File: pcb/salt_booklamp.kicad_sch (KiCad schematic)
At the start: 26 parts, among them J1 USB-C31-S-RA-CS1E-BK-T/R, P1 PIC-TC2050-IDC, U1 PIC16F15213-I/SN, U2 BQ21040DBVR, U3 TPS61158DRVR

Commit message: Add CC resistors to schematic for USB compliant smart chargers
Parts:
- added R10, R9: 5k1, salt_booklamp_footprints:res_0603, symbol salt_booklamp:resistor
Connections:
- net GND: now also R10.2, R9.2
- net at J1.A5 (CC1): now also R9.1
- net at J1.B5 (CC2): now also R10.1
- no-connect marks 17 -> 15

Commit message: Changed 0603 parts to 0402, assigned 0402 uF cap MPN, still need to assign 0402 Resistor MPNs
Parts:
- C1, C2, C3, C4, C5: footprint salt_booklamp_footprints:cap_0603 -> Capacitor_SMD:C_0402_1005Metric; Manufacturer Part Number CL10B105KP8NNNC -> EMK105BJ105KV-F
- R1, R10, R2, R3, R4, R5, R6, R7, R8, R9: footprint salt_booklamp_footprints:res_0603 -> Resistor_SMD:R_0402_1005Metric
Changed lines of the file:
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@@
 		)
 	)
-	(text_box "PENDING CHANGES Rev 0.2\n----------------------\n[ ]-Measure Battery Voltage? - move measurement to different pin\n\n[X]-Add another LED\n\n[ ]-Battery Connector\n\n[X]-USBC - 5k1 R from CC to GND\n\n[ ]-0402 components for more space\n\n"
+	(text_box "PENDING CHANGES Rev 0.2\n----------------------\n[ ]-Measure Battery Voltage? - move measurement to different pin\n\n[X]-Add another LED\n\n[ ]-Battery Connector\n\n[X]-USBC - 5k1 R from CC to GND\n\n[X]-0402 components for more space\n\n"
 		(exclude_from_sim no)
 		(at 27.94 153.67 0)
@@
 			"AAAAAAAAAAAAAAAAAAAAAAAAAAAAAAAAAAAAAAAAAAAAAAAAAAAAAAAAAAAAAAAAAAAAAAAAAAAA"
 			"AAAAAAAAAAAAAAAAAAAAAAAAAAAAAAAAAAAAAAAAAAAAAAAAAAAAAAAAAAAAAAAAAAAAAAAAAAAA"
+			"AAAAAAAAAAAAAAAAAAAAAAAAAAAAAAAAAAAAAAAAAAAAAAAAAAAAAAAAAAAAAAAAAAAAAAAAAAAA"
+			"AAAAAAAAAAAAAAAAAAAAAAAAAAAAAAAAAAAAAAAAAAAAAAAAAAAAAAAAAAAAAAAAAAAAAAAAAAAA"
+			"AAAAAAAAAAAAAAAAAAAAAAAAAAAAAAAAAAAAAAAAAAAAAAAAAAAAAAAAAAAAAAAAAAAAAAAAAAAA"
+			"AAAAAAAAAAAAAAAAAAAAAAAAAAAAAAAAAAAAAAAAAAAAAAAAAAAAAAAAAAAAAAAAAAAAAAAAAAAA"
+			"AAAAAAAAAAAAAAAAAAAAAAAAAAAAAAAAAAAAAAAAAAAAAAAAAAAAAAAAAAAAAAAAAAAAAAAAAAAA"
+			"AAAAAAAAAAAAAAAAAAAAAAAAAAAAAAAAAAAAAAAAAAAAAAAAAAAAAAAAAAAAAAAAAAAAAAAAAAAA"
+			"AAAAAAAAAAAAAAAAAAAAAAAAAAAAAAAAAAAAAAAAAAAAAAAAAAAAAAAAAAAAAAAAAAAAAAAAAAAA"
+			"AAAAAAAAAAAAAAAAAAAAAAAAAAAAAAAAAAAAAAAAAAAAAAAAAAAAAAAAAAAAAAAAAAAAAAAAAAAA"
+			"AAAAAAAAAAAAAAAAAAAAAAAAAAAAAAAAAAAAAAAAAAAAAAAAAAAAAAAAAAAAAAAAAAAAAAAAAAAA"
+			"AAAAAAAAAAAAAAAAAAAAAAAAAAAAAAAAAAAAAAAAAAAAAAAAAAAAAAAAAAAAAAAAAAAAAAAAAAAA"
+			"AAAAAAAAAAAAAAAAAAAAAAAAAAAAAAAAAAAAAAAAAAAAAAAAAAAAAAAAAAAAAAAAAAAAAAAAAAAA"
+			"AAAAAAAAAAAAAAAAAAAAAAAAAAAAAAAAAAAAAAAAAAAAAAAAAAAAAAAAAAAAAAAAAAAAAAAAAAAA"
+			"AAAAAAAAAAAAAAAAAAAAAAAAAAAAAAAAAAAAAAAAAAAAAAAAAAAAAAAAAAAAAAAAAAAAAAAAAAAA"
+			"AAAAAAAAAAAAAAAAAAAAAAAAAAAAAAAAAAAAAAAAAAAAAAAAAAAAAAAAAAAAAAAAAAAAAAAAAAAA"
+			"AAAAAAAAAAAAAAAAAAAAAAAAAAAAAAAAAAAAAAAAAAAAAAAAAAAAAAAAAAAAAAAAAAAAAAAAAAAA"
+			"AAAAAAAAAAAAAAAAAAAAAAAAAAAAAAAAAAAAAAAAAAAAAAAAAAAAAAAAAAAAAAAAAAAAAAAAAAAA"
+			"AAAAAAAAAAAAAAAAAAAAAAAAAAAAAAAAAAAAAAAAAAAAAAAAAAAAAAAAAAAAAAAAAAAAAAAAAAAA"
+			"AAAAAAAAAAAAAAAAAAAAAAAAAAAAAAAAAAAAAAAAAAAAAAAAAAAAAAAAAAAAAAAAAAAAAAAAAAAA"
 			"AAAAAAAAAA=="
 		)
@@
 			)
 		)
-		(property "Footprint" "salt_booklamp_footprints:res_0603"
+		(property "Footprint" "Resistor_SMD:R_0402_1005Metric"
 			(at 134.62 134.62 0)
 			(effects
@@
 			)
 		)
-		(property "Footprint" "salt_booklamp_footprints:res_0603"
+		(property "Footprint" "Resistor_SMD:R_0402_1005Metric"
 			(at 158.75 91.44 0)
 			(effects
@@
 			)
 		)
-		(property "Footprint" "salt_booklamp_footprints:res_0603"
+		(property "Footprint" "Resistor_SMD:R_0402_1005Metric"
 			(at 252.73 128.27 0)
 			(effects
@@
 			)
 		)
-		(property "Footprint" "salt_booklamp_footprints:cap_0603"
+		(property "Footprint" "Capacitor_SMD:C_0402_1005Metric"
 			(at 219.71 109.22 0)
 			(effects
@@
 			)
 		)
-		(property "Description" "CAP CER 1UF 10V X7R 0603"
+		(property "Description" "CAP CER 1UF 16V X5R 0402"
 			(at 219.71 104.14 0)
 			(effects
@@
 			)
 		)
-		(property "Manufacturer Part Number" "CL10B105KP8NNNC"
+		(property "Manufacturer Part Number" "EMK105BJ105KV-F"
 			(at 209.804 98.298 0)
 			(effects
@@
 			)
 		)
-		(property "Footprint" "salt_booklamp_footprints:cap_0603"
+		(property "Footprint" "Capacitor_SMD:C_0402_1005Metric"
 			(at 55.88 97.79 0)
 			(effects
@@
 			)
 		)
-		(property "Description" "CAP CER 1UF 10V X7R 0603"
+		(property "Description" "CAP CER 1UF 16V X5R 0402"
 			(at 55.88 92.71 0)
 			(effects
@@
 			)
 		)
-		(property "Manufacturer Part Number" "CL10B105KP8NNNC"
+		(property "Manufacturer Part Number" "EMK105BJ105KV-F"
 			(at 55.88 92.71 0)
 			(effects
@@
 			)
 		)
-		(property "Footprint" "salt_booklamp_footprints:res_0603"
+		(property "Footprint" "Resistor_SMD:R_0402_1005Metric"
 			(at 92.71 119.38 0)
 			(effects
@@
 			)
 		)
-		(property "Footprint" "salt_booklamp_footprints:cap_0603"
+		(property "Footprint" "Capacitor_SMD:C_0402_1005Metric"
 			(at 151.13 125.73 0)
 			(effects
@@
 			)
 		)
-		(property "Description" "CAP CER 1UF 10V X7R 0603"
+		(property "Description" "CAP CER 1UF 16V X5R 0402"
 			(at 151.13 120.65 0)
 			(effects
@@
 			)
 		)
-		(property "Manufacturer Part Number" "CL10B105KP8NNNC"
+		(property "Manufacturer Part Number" "EMK105BJ105KV-F"
 			(at 151.13 120.65 0)
 			(effects
@@
 			)
 		)
-		(property "Footprint" "salt_booklamp_footprints:res_0603"
+		(property "Footprint" "Resistor_SMD:R_0402_1005Metric"
 			(at 59.69 120.65 0)
 			(effects
@@
 			)
 		)
-		(property "Footprint" "salt_booklamp_footprints:res_0603"
+		(property "Footprint" "Resistor_SMD:R_0402_1005Metric"
 			(at 125.73 95.25 0)
 			(effects
@@
 			)
 		)
-		(property "Footprint" "salt_booklamp_footprints:cap_0603"
+		(property "Footprint" "Capacitor_SMD:C_0402_1005Metric"
 			(at 107.95 99.06 0)
 			(effects
@@
 			)
 		)
-		(property "Description" "CAP CER 1UF 10V X7R 0603"
+		(property "Description" "CAP CER 1UF 16V X5R 0402"
 			(at 107.95 93.98 0)
 			(effects
@@
 			)
 		)
-		(property "Manufacturer Part Number" "CL10B105KP8NNNC"
+		(property "Manufacturer Part Number" "EMK105BJ105KV-F"
 			(at 107.95 93.98 0)
 			(effects
@@
 			)
 		)
-		(property "Footprint" "salt_booklamp_footprints:cap_0603"
+		(property "Footprint" "Capacitor_SMD:C_0402_1005Metric"
 			(at 257.81 119.38 0)
 			(effects
@@
 			)
 		)
-		(property "Description" "CAP CER 1UF 10V X7R 0603"
+		(property "Description" "CAP CER 1UF 16V X5R 0402"
 			(at 257.81 114.3 0)
 			(effects
@@
 			)
 		)
-		(property "Manufacturer Part Number" "CL10B105KP8NNNC"
+		(property "Manufacturer Part Number" "EMK105BJ105KV-F"
 			(at 257.81 114.3 0)
 			(effects
@@
 			)
 		)
-		(property "Footprint" "salt_booklamp_footprints:res_0603"
+		(property "Footprint" "Resistor_SMD:R_0402_1005Metric"
 			(at 133.35 95.25 0)
 			(effects
@@
 			)
 		)
-		(property "Footprint" "salt_booklamp_footprints:res_0603"
+		(property "Footprint" "Resistor_SMD:R_0402_1005Metric"
 			(at 15.24 111.76 0)
 			(effects
@@
 			)
 		)
-		(property "Footprint" "salt_booklamp_footprints:res_0603"
+		(property "Footprint" "Resistor_SMD:R_0402_1005Metric"
 			(at 10.16 111.76 0)
 			(effects
@@
 			)
 		)
-		(property "Footprint" "salt_booklamp_footprints:res_0603"
+		(property "Footprint" "Resistor_SMD:R_0402_1005Metric"
 			(at 273.05 123.19 0)
 			(effects

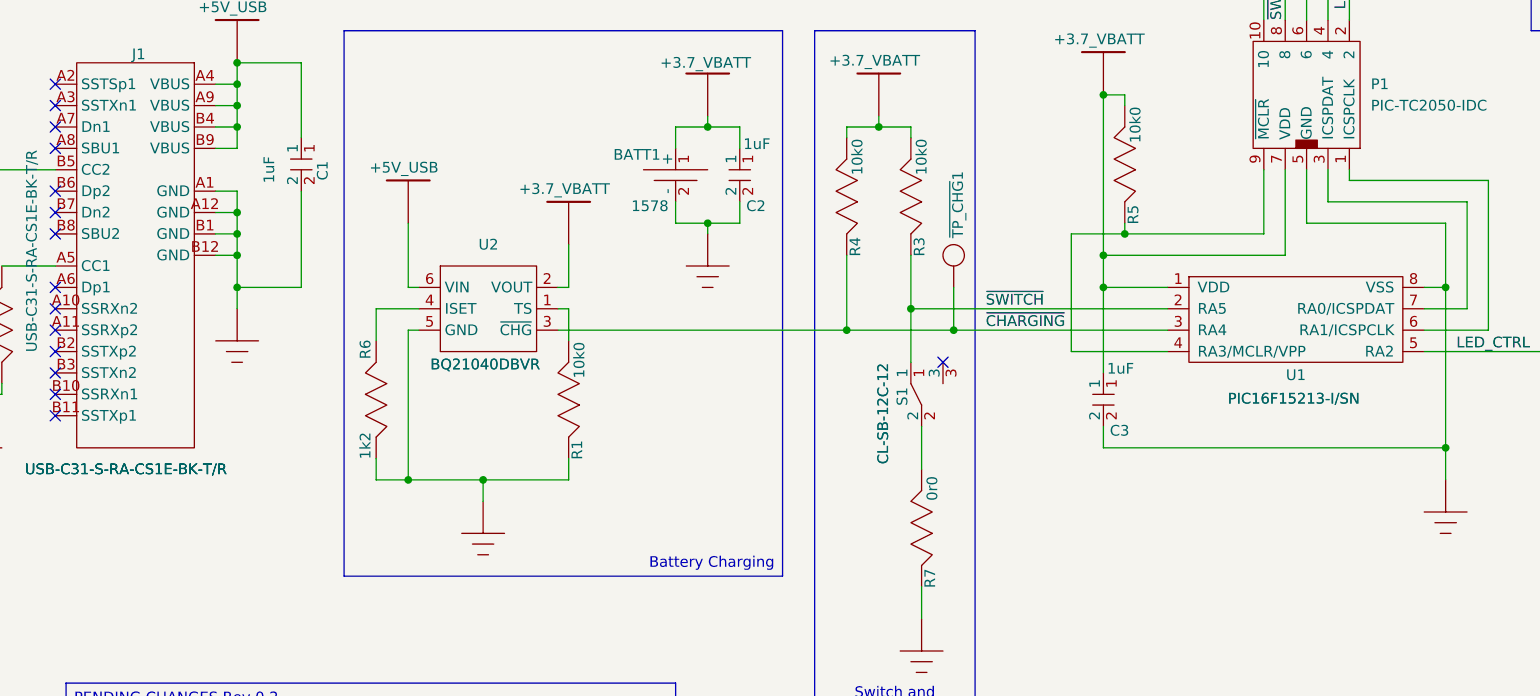
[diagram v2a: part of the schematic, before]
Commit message: Changed MCU to smaller DFN package, add Connector footprint to PCB (very big), add shield pins to USB footprint to remove warning
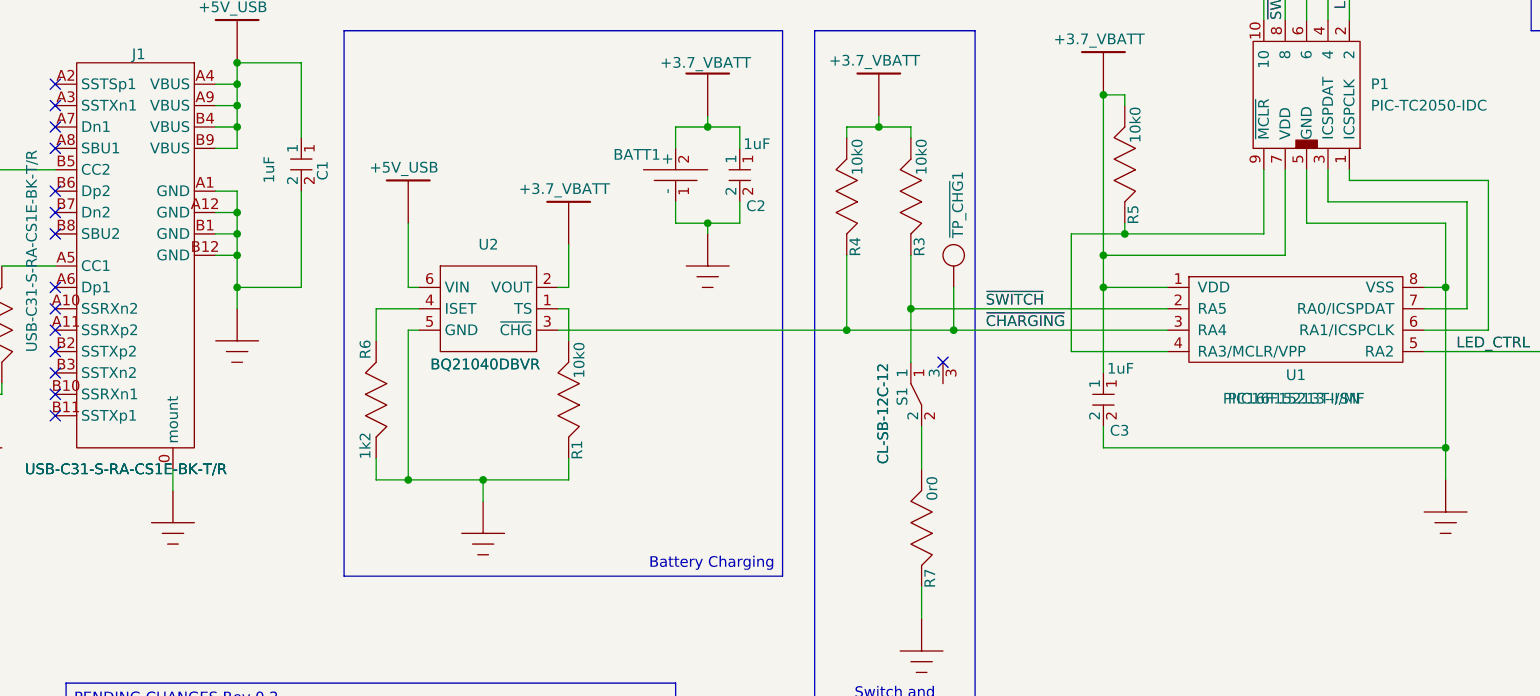
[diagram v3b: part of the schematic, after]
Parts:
- BATT1: value 1578 -> S2B-PH-K-S; footprint salt_booklamp_footprints:PRT-13851 -> GymTimer:JST_PH_S2B-PH-K_1x02_P2.00mm_Horizontal; Manufacturer Part Number (none) -> S2B-PH-K-S; now in the parts list
- U1: footprint salt_booklamp_footprints:SOIC-8 - PIC16F15213 -> GymTimer:DFN-8-1EP_3x3mm_P0.65mm_EP1.55x2.4mm; Digikey https://www.digikey.com/en/products/detail/microchip-technology/PIC16F15213-I-SN/12807336 -> https://www.digikey.com/en/products/detail/microchip-technology/PIC16F15213T-I-MF/12807572; Manufacturer Part Number PIC16F15213-I/SN -> PIC16F15213T-I/MF
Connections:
- net +3.7_VBATT: now also BATT1.2 (+); no longer BATT1.1 (+)
- net GND: now also BATT1.1 (-), J1.0 (mount); no longer BATT1.2 (-)
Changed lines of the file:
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@@
 	(wire
 		(pts
+			(xy 40.64 128.27) (xy 40.64 130.81)
+		)
+		(stroke
+			(width 0)
+			(type default)
+		)
+	)
+	(wire
+		(pts
 			(xy 194.31 109.22) (xy 194.31 96.52)
 		)
@@
 			"AAAAAAAAAAAAAAAAAAAAAAAAAAAAAAAAAAAAAAAAAAAAAAAAAAAAAAAAAAAAAAAAAAAAAAAAAAAA"
 			"AAAAAAAAAAAAAAAAAAAAAAAAAAAAAAAAAAAAAAAAAAAAAAAAAAAAAAAAAAAAAAAAAAAAAAAAAAAA"
+			"AAAAAAAAAAAAAAAAAAAAAAAAAAAAAAAAAAAAAAAAAAAAAAAAAAAAAAAAAAAAAAAAAAAAAAAAAAAA"
+			"AAAAAAAAAAAAAAAAAAAAAAAAAAAAAAAAAAAAAAAAAAAAAAAAAAAAAAAAAAAAAAAAAAAAAAAAAAAA"
+			"AAAAAAAAAAAAAAAAAAAAAAAAAAAAAAAAAAAAAAAAAAAAAAAAAAAAAAAAAAAAAAAAAAAAAAAAAAAA"
+			"AAAAAAAAAAAAAAAAAAAAAAAAAAAAAAAAAAAAAAAAAAAAAAAAAAAAAAAAAAAAAAAAAAAAAAAAAAAA"
+			"AAAAAAAAAAAAAAAAAAAAAAAAAAAAAAAAAAAAAAAAAAAAAAAAAAAAAAAAAAAAAAAAAAAAAAAAAAAA"
+			"AAAAAAAAAAAAAAAAAAAAAAAAAAAAAAAAAAAAAAAAAAAAAAAAAAAAAAAAAAAAAAAAAAAAAAAAAAAA"
+			"AAAAAAAAAAAAAAAAAAAAAAAAAAAAAAAAAAAAAAAAAAAAAAAAAAAAAAAAAAAAAAAAAAAAAAAAAAAA"
+			"AAAAAAAAAAAAAAAAAAAAAAAAAAAAAAAAAAAAAAAAAAAAAAAAAAAAAAAAAAAAAAAAAAAAAAAAAAAA"
+			"AAAAAAAAAAAAAAAAAAAAAAAAAAAAAAAAAAAAAAAAAAAAAAAAAAAAAAAAAAAAAAAAAAAAAAAAAAAA"
+			"AAAAAAAAAAAAAAAAAAAAAAAAAAAAAAAAAAAAAAAAAAAAAAAAAAAAAAAAAAAAAAAAAAAAAAAAAAAA"
+			"AAAAAAAAAAAAAAAAAAAAAAAAAAAAAAAAAAAAAAAAAAAAAAAAAAAAAAAAAAAAAAAAAAAAAAAAAAAA"
+			"AAAAAAAAAAAAAAAAAAAAAAAAAAAAAAAAAAAAAAAAAAAAAAAAAAAAAAAAAAAAAAAAAAAAAAAAAAAA"
+			"AAAAAAAAAAAAAAAAAAAAAAAAAAAAAAAAAAAAAAAAAAAAAAAAAAAAAAAAAAAAAAAAAAAAAAAAAAAA"
+			"AAAAAAAAAAAAAAAAAAAAAAAAAAAAAAAAAAAAAAAAAAAAAAAAAAAAAAAAAAAAAAAAAAAAAAAAAAAA"
+			"AAAAAAAAAAAAAAAAAAAAAAAAAAAAAAAAAAAAAAAAAAAAAAAAAAAAAAAAAAAAAAAAAAAAAAAAAAAA"
+			"AAAAAAAAAAAAAAAAAAAAAAAAAAAAAAAAAAAAAAAAAAAAAAAAAAAAAAAAAAAAAAAAAAAAAAAAAAAA"
+			"AAAAAAAAAAAAAAAAAAAAAAAAAAAAAAAAAAAAAAAAAAAAAAAAAAAAAAAAAAAAAAAAAAAAAAAAAAAA"
+			"AAAAAAAAAAAAAAAAAAAAAAAAAAAAAAAAAAAAAAAAAAAAAAAAAAAAAAAAAAAAAAAAAAAAAAAAAAAA"
+			"AAAAAAAAAAAAAAAAAAAAAAAAAAAAAAAAAAAAAAAAAAAAAAAAAAAAAAAAAAAAAAAAAAAAAAAAAAAA"
+			"AAAAAAAAAAAAAAAAAAAAAAAAAAAAAAAAAAAAAAAAAAAAAAAAAAAAAAAAAAAAAAAAAAAAAAAAAAAA"
+			"AAAAAAAAAAAAAAAAAAAAAAAAAAAAAAAAAAAAAAAAAAAAAAAAAAAAAAAAAAAAAAAAAAAAAAAAAAAA"
+			"AAAAAAAAAAAAAAAAAAAAAAAAAAAAAAAAAAAAAAAAAAAAAAAAAAAAAAAAAAAAAAAAAAAAAAAAAAAA"
+			"AAAAAAAAAAAAAAAAAAAAAAAAAAAAAAAAAAAAAAAAAAAAAAAAAAAAAAAAAAAAAAAAAAAAAAAAAAAA"
+			"AAAAAAAAAAAAAAAAAAAAAAAAAAAAAAAAAAAAAAAAAAAAAAAAAAAAAAAAAAAAAAAAAAAAAAAAAAAA"
+			"AAAAAAAAAAAAAAAAAAAAAAAAAAAAAAAAAAAAAAAAAAAAAAAAAAAAAAAAAAAAAAAAAAAAAAAAAAAA"
+			"AAAAAAAAAAAAAAAAAAAAAAAAAAAAAAAAAAAAAAAAAAAAAAAAAAAAAAAAAAAAAAAAAAAAAAAAAAAA"
+			"AAAAAAAAAAAAAAAAAAAAAAAAAAAAAAAAAAAAAAAAAAAAAAAAAAAAAAAAAAAAAAAAAAAAAAAAAAAA"
+			"AAAAAAAAAAAAAAAAAAAAAAAAAAAAAAAAAAAAAAAAAAAAAAAAAAAAAAAAAAAAAAAAAAAAAAAAAAAA"
+			"AAAAAAAAAAAAAAAAAAAAAAAAAAAAAAAAAAAAAAAAAAAAAAAAAAAAAAAAAAAAAAAAAAAAAAAAAAAA"
+			"AAAAAAAAAAAAAAAAAAAAAAAAAAAAAAAAAAAAAAAAAAAAAAAAAAAAAAAAAAAAAAAAAAAAAAAAAAAA"
+			"AAAAAAAAAAAAAAAAAAAAAAAAAAAAAAAAAAAAAAAAAAAAAAAAAAAAAAAAAAAAAAAAAAAAAAAAAAAA"
+			"AAAAAAAAAAAAAAAAAAAAAAAAAAAAAAAAAAAAAAAAAAAAAAAAAAAAAAAAAAAAAAAAAAAAAAAAAAAA"
+			"AAAAAAAAAAAAAAAAAAAAAAAAAAAAAAAAAAAAAAAAAAAAAAAAAAAAAAAAAAAAAAAAAAAAAAAAAAAA"
+			"AAAAAAAAAAAAAAAAAAAAAAAAAAAAAAAAAAAAAAAAAAAAAAAAAAAAAAAAAAAAAAAAAAAAAAAAAAAA"
+			"AAAAAAAAAAAAAAAAAAAAAAAAAAAAAAAAAAAAAAAAAAAAAAAAAAAAAAAAAAAAAAAAAAAAAAAAAAAA"
+			"AAAAAAAAAAAAAAAAAAAAAAAAAAAAAAAAAAAAAAAAAAAAAAAAAAAAAAAAAAAAAAAAAAAAAAAAAAAA"
 			"AAAAAAAAAA=="
 		)
@@
 		(pin "B2"
 		)
+		(pin "0"
+		)
 		(instances
 			(project "salt_booklamp"
@@
 		(unit 1)
 		(exclude_from_sim yes)
-		(in_bom no)
+		(in_bom yes)
 		(on_board yes)
 		(dnp no)
@@
 			)
 		)
-		(property "Value" "1578"
+		(property "Value" "S2B-PH-K-S"
 			(at 97.282 97.028 0)
 			(effects
@@
 					(size 1.27 1.27)
 				)
+				(hide yes)
+			)
+		)
+		(property "Footprint" "GymTimer:JST_PH_S2B-PH-K_1x02_P2.00mm_Horizontal"
+			(at 100.33 93.98 0)
+			(effects
+				(font
+					(size 1.27 1.27)
+				)
+				(hide yes)
 			)
 		)
-		(property "Footprint" "salt_booklamp_footprints:PRT-13851"
+		(property "Datasheet" "https://www.digikey.com/en/products/detail/jst-sales-america-inc/S2B-PH-K-S/926626"
 			(at 100.33 93.98 0)
 			(effects
@@
 			)
 		)
-		(property "Datasheet" "https://www.digikey.com/en/products/detail/adafruit-industries-llc/1578/5054539"
+		(property "Description" "CONN HEADER R/A 2POS 2MM"
 			(at 100.33 93.98 0)
 			(effects
@@
 			)
 		)
-		(property "Description" "BATTERY LITH-ION 3.7V 500MAH"
+		(property "Manufacturer Part Number" "S2B-PH-K-S"
 			(at 100.33 93.98 0)
 			(effects
@@
 	)
 	(symbol
+		(lib_name "P,GND_2")
+		(lib_id "PCM_Generic:P,GND")
+		(at 40.64 130.81 0)
+		(unit 1)
+		(exclude_from_sim yes)
+		(in_bom yes)
+		(on_board yes)
+		(dnp no)
+		(fields_autoplaced yes)
+		(property "Reference" "#PWR020"
+			(at 44.45 127 0)
+			(effects
+				(font
+					(size 2.54 2.54)
+				)
+				(justify left)
+				(hide yes)
+			)
+		)
+		(property "Value" "GND"
+			(at 44.45 130.81 0)
+			(effects
+				(font
+					(size 0.0254 0.0254)
+				)
+				(justify left)
+				(hide yes)
+			)
+		)
+		(property "Footprint" ""
+			(at 40.64 130.81 0)
+			(effects
+				(font
+					(size 2.54 2.54)
+				)
+				(hide yes)
+			)
+		)
+		(property "Datasheet" ""
+			(at 40.64 130.81 0)
+			(effects
+				(font
+					(size 2.54 2.54)
+				)
+				(hide yes)
+			)
+		)
+		(property "Description" ""
+			(at 40.64 130.81 0)
+			(effects
+				(font
+					(size 1.27 1.27)
+				)
+				(hide yes)
+			)
+		)
+		(pin "0"
+		)
+		(instances
+			(project "salt_booklamp"
+				(path "/991f2cc7-99ce-452c-919d-a53cd26a4b08"
+					(reference "#PWR020")
+					(unit 1)
+				)
+			)
+		)
+	)
+	(symbol
 		(lib_id "salt_booklamp:Power")
 		(at 219.71 92.71 0)
@@
 			)
 		)
-		(property "Footprint" "salt_booklamp_footprints:SOIC-8 - PIC16F15213"
+		(property "Footprint" "GymTimer:DFN-8-1EP_3x3mm_P0.65mm_EP1.55x2.4mm"
 			(at 166.37 111.76 0)
 			(effects
@@
 			)
 		)
-		(property "Digikey" "https://www.digikey.com/en/products/detail/microchip-technology/PIC16F15213-I-SN/12807336"
+		(property "Digikey" "https://www.digikey.com/en/products/detail/microchip-technology/PIC16F15213T-I-MF/12807572"
 			(at 173.99 110.49 0)
 			(effects
@@
 			)
 		)
-		(property "Manufacturer Part Number" "PIC16F15213-I/SN"
+		(property "Manufacturer Part Number" "PIC16F15213T-I/MF"
 			(at 173.736 119.888 0)
 			(effects
